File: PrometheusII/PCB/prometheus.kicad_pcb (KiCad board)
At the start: 4 copper layers, 223.5 x 222.3 mm, 240 parts, among them J1 0878311420, J10 Conn_02x02_Odd_Even, J11 Conn_02x02_Odd_Even, J12 Conn_02x08_Odd_Even, J13 Conn_02x08_Odd_Even, J14 Conn_02x08_Odd_Even, J2 Conn_02x08_Odd_Even, J3 Conn_02x02_Odd_Even, J4 Conn_02x02_Odd_Even, J7 Conn_02x08_Odd_Even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

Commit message: Base logic for arc completion works?
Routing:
- net (no net): track 368.4 -> 387.0 mm
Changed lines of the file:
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@@
   (general
     (thickness 1.6)
-    (drawings 239)
-    (tracks 687)
+    (drawings 240)
+    (tracks 689)
     (zones 0)
     (modules 240)
@@
     )
   )
+  (gr_arc (start 99.054 138.009) (end 99.689 136.485) (angle -99.62521694) (layer F.Cu) (width 0.16))
   (gr_circle (center 102.746 98.016) (end 106.646 98.016) (layer B.SilkS) (width 0.16))
   (gr_circle (center 102.746 98.016) (end 106.336 98.016) (layer B.SilkS) (width 0.16))
@@
   (gr_circle (center 106.2735 138.938) (end 107.8435 138.938) (layer B.Cu) (width 0.16))
   (gr_circle (center 106.2735 138.938) (end 107.5235 138.938) (layer B.Cu) (width 0.16))
-  (gr_arc (start 98.9329 138.0998) (end 99.8473 136.6774) (angle 147.2597811) (layer B.Cu) (width 0.16))
+  (gr_arc (start 98.9329 138.0998) (end 99.8473 136.6774) (angle 249.0202197) (layer B.Cu) (width 0.16))
   (gr_arc (start 99.4663 130.8608) (end 100.3807 129.4384) (angle 147.2597811) (layer B.Cu) (width 0.16))
   (gr_arc (start 99.2377 131.2672) (end 99.2377 129.9972) (angle -90) (layer B.Cu) (width 0.16))
@@
   (segment (start 70.198799 115.605993) (end 85.206657 119.741104) (width 0.16) (layer F.Cu) (net 85))
   (segment (start 70.113797 115.914497) (end 85.121655 120.049608) (width 0.16) (layer F.Cu) (net 0))
+  (segment (start 86.750967 139.302139) (end 77.688432 138.62466) (width 0.15) (layer B.Cu) (net 0))
+  (segment (start 86.676185 144.222117) (end 77.255214 143.102682) (width 0.15) (layer B.Cu) (net 0))
   (segment (start 71.108775 101.323762) (end 100.557255 95.046046) (width 0.16) (layer F.Cu) (net 72))
   (segment (start 71.175492 101.636729) (end 100.623973 95.359014) (width 0.16) (layer F.Cu) (net 1))

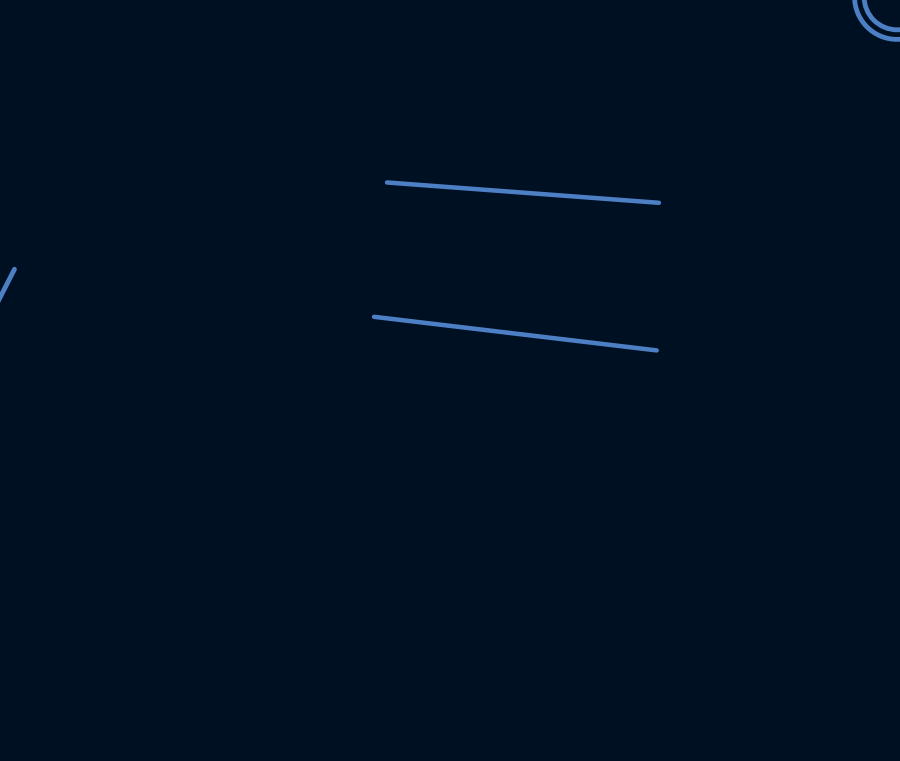
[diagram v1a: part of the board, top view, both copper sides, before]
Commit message: Cleaned up node dialog and added layer select
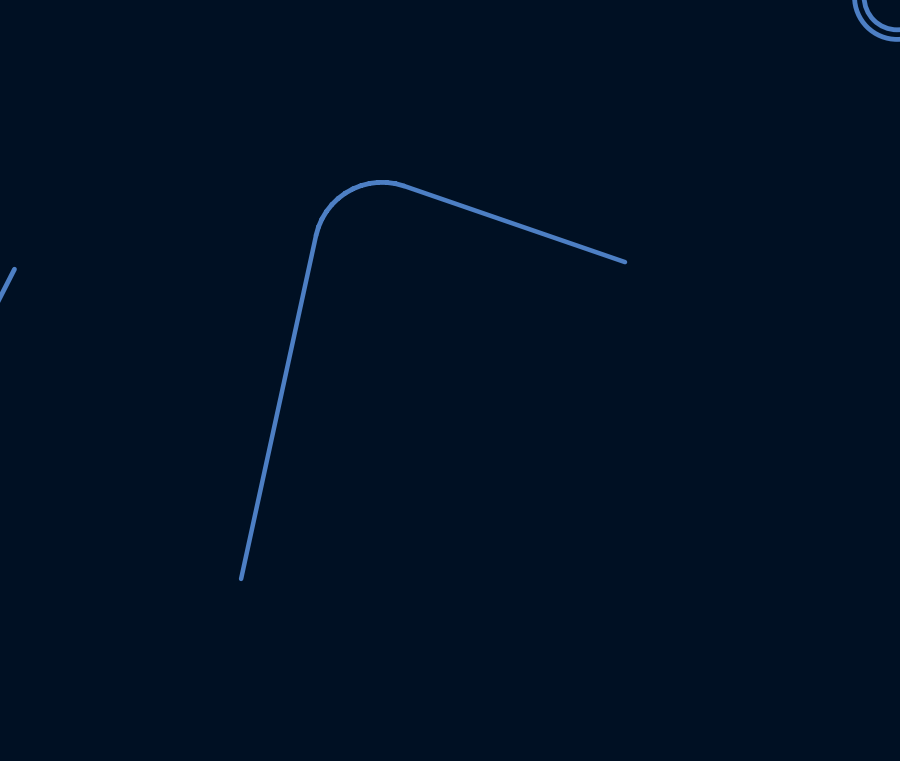
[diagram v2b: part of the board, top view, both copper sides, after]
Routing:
- net +5V: track 41.0 -> 48.8 mm
- net (no net): track 387.0 -> 383.9 mm
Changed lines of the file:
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@@
     (thickness 1.6)
     (drawings 240)
-    (tracks 689)
+    (tracks 702)
     (zones 0)
     (modules 240)
@@
     (35 F.Paste user hide)
     (36 B.SilkS user)
-    (37 F.SilkS user hide)
+    (37 F.SilkS user)
     (38 B.Mask user)
     (39 F.Mask user)
@@
     (44 Edge.Cuts user)
     (45 Margin user)
-    (46 B.CrtYd user)
-    (47 F.CrtYd user)
+    (46 B.CrtYd user hide)
+    (47 F.CrtYd user hide)
     (48 B.Fab user hide)
     (49 F.Fab user hide)
@@
     (solder_mask_min_width 0.25)
     (aux_axis_origin 156.456 180.632)
-    (grid_origin 87.751 140.803)
+    (grid_origin 124.708 144.232)
     (visible_elements 7FFFFFFF)
     (pcbplotparams
@@
   (gr_circle (center 79.7455 125.69) (end 82.4955 125.69) (layer B.SilkS) (width 0.16))
   (gr_circle (center 42.92092 133.598) (end 43.92092 133.598) (layer F.Cu) (width 0.16))
-  (gr_circle (center 86.9187 137.0584) (end 89.1687 137.0584) (layer B.SilkS) (width 0.16))
+  (gr_circle (center 86.354 139.152) (end 88.604 139.152) (layer B.SilkS) (width 0.16))
   (gr_circle (center 86.4107 146.4564) (end 88.6607 146.4564) (layer B.SilkS) (width 0.16))
   (gr_circle (center 77.5207 140.8684) (end 79.7707 140.8684) (layer B.SilkS) (width 0.16))
@@
   (segment (start 70.198799 115.605993) (end 85.206657 119.741104) (width 0.16) (layer F.Cu) (net 85))
   (segment (start 70.113797 115.914497) (end 85.121655 120.049608) (width 0.16) (layer F.Cu) (net 0))
-  (segment (start 86.750967 139.302139) (end 77.688432 138.62466) (width 0.15) (layer B.Cu) (net 0))
-  (segment (start 86.676185 144.222117) (end 77.255214 143.102682) (width 0.15) (layer B.Cu) (net 0))
+  (segment (start 85.621124 141.279297) (end 78.253575 138.741102) (width 0.15) (layer B.Cu) (net 7))
+  (segment (start 72.823349 151.839474) (end 75.322443 140.38864) (width 0.15) (layer B.Cu) (net 0))
+  (segment (start 78.253574 138.741102) (end 77.972011 138.664127) (width 0.16) (layer B.Cu) (net 0))
+  (segment (start 77.972011 138.664127) (end 77.682851 138.62425) (width 0.16) (layer B.Cu) (net 0))
+  (segment (start 77.682851 138.62425) (end 77.390963 138.622143) (width 0.16) (layer B.Cu) (net 0))
+  (segment (start 77.390963 138.622143) (end 77.101258 138.657841) (width 0.16) (layer B.Cu) (net 0))
+  (segment (start 77.101258 138.657841) (end 76.818612 138.730743) (width 0.16) (layer B.Cu) (net 0))
+  (segment (start 76.818612 138.730743) (end 76.547783 138.839623) (width 0.16) (layer B.Cu) (net 0))
+  (segment (start 76.547783 138.839623) (end 76.293328 138.982648) (width 0.16) (layer B.Cu) (net 0))
+  (segment (start 76.293328 138.982648) (end 76.05953 139.15741) (width 0.16) (layer B.Cu) (net 0))
+  (segment (start 76.05953 139.15741) (end 75.850324 139.360969) (width 0.16) (layer B.Cu) (net 0))
+  (segment (start 75.850324 139.360969) (end 75.669231 139.589898) (width 0.16) (layer B.Cu) (net 0))
+  (segment (start 75.669231 139.589898) (end 75.519299 139.840345) (width 0.16) (layer B.Cu) (net 0))
+  (segment (start 75.519299 139.840345) (end 75.403051 140.108094) (width 0.16) (layer B.Cu) (net 0))
+  (segment (start 75.403051 140.108094) (end 75.322443 140.38864) (width 0.16) (layer B.Cu) (net 0))
   (segment (start 71.108775 101.323762) (end 100.557255 95.046046) (width 0.16) (layer F.Cu) (net 72))
   (segment (start 71.175492 101.636729) (end 100.623973 95.359014) (width 0.16) (layer F.Cu) (net 1))

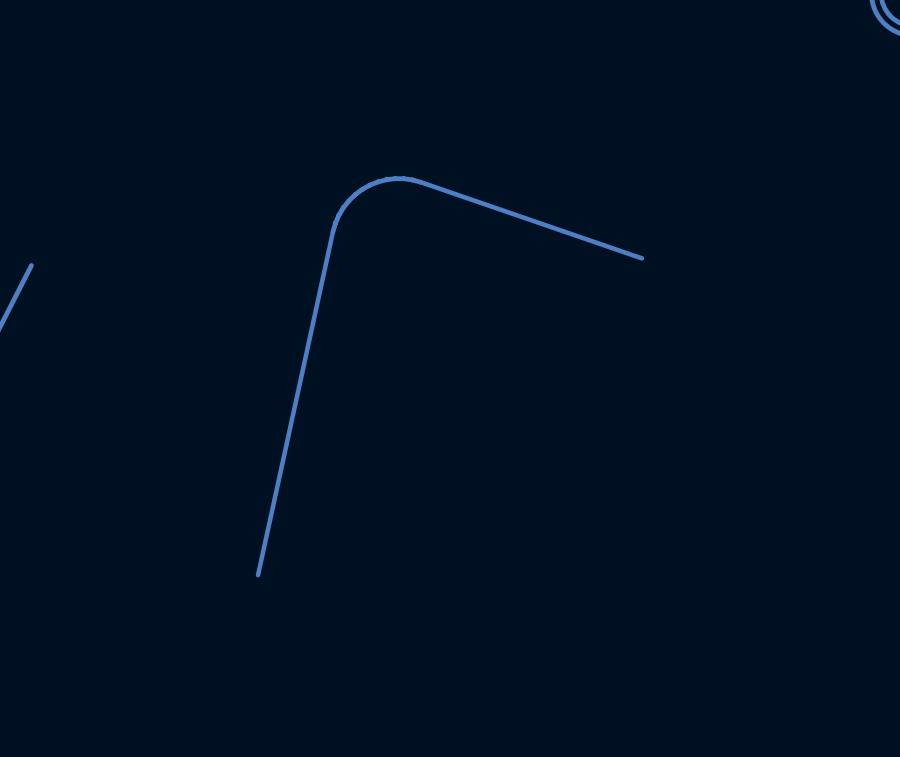
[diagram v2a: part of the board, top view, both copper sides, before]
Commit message: Refactor bus tangent finding to allow for including layers
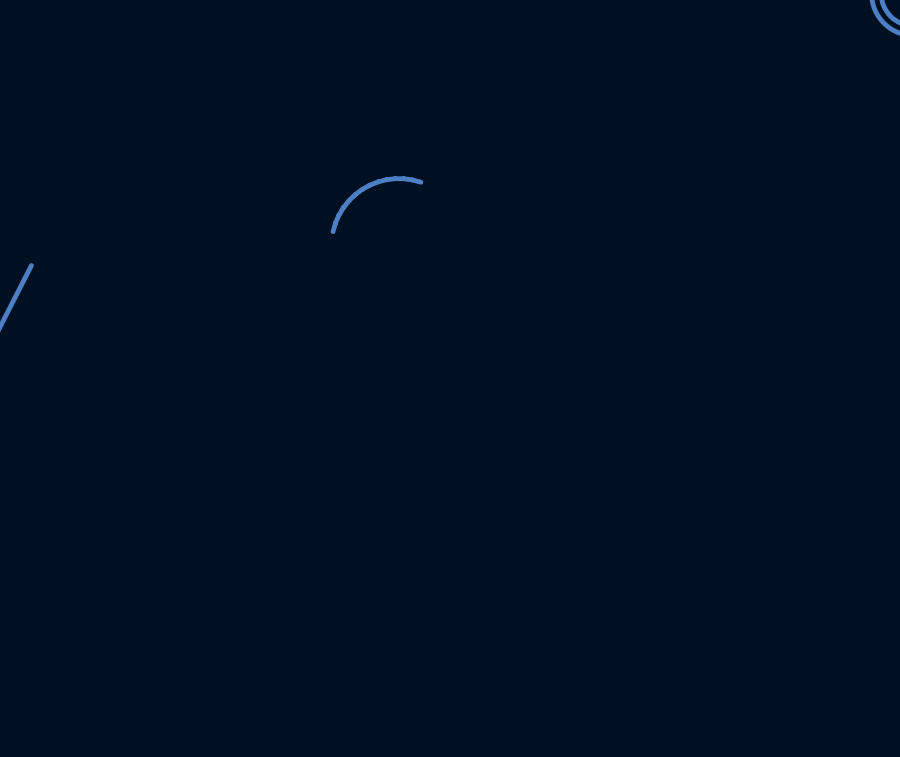
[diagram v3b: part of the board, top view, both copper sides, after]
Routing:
- net (no net): track 383.9 -> 372.2 mm
- net +5V: track 48.8 -> 41.0 mm
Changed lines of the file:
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@@
   (general
     (thickness 1.6)
-    (drawings 240)
-    (tracks 702)
+    (drawings 245)
+    (tracks 700)
     (zones 0)
     (modules 240)
@@
     (solder_mask_min_width 0.25)
     (aux_axis_origin 156.456 180.632)
-    (grid_origin 124.708 144.232)
+    (grid_origin 72.892 145.883)
     (visible_elements 7FFFFFFF)
     (pcbplotparams
@@
     )
   )
+  (gr_circle (center 89.5857 140.2334) (end 92.1557 140.2334) (layer B.SilkS) (width 0.16))
+  (gr_circle (center 89.5857 140.2334) (end 91.8357 140.2334) (layer B.SilkS) (width 0.16))
+  (gr_circle (center 79.8067 149.6314) (end 82.6967 149.6314) (layer B.SilkS) (width 0.16))
+  (gr_circle (center 79.8067 149.6314) (end 82.3767 149.6314) (layer B.SilkS) (width 0.16))
+  (gr_circle (center 79.8067 149.6314) (end 82.0567 149.6314) (layer B.SilkS) (width 0.16))
+  (gr_circle (center 88.8237 148.8694) (end 91.7137 148.8694) (layer B.SilkS) (width 0.16))
+  (gr_circle (center 88.8237 148.8694) (end 91.3937 148.8694) (layer B.SilkS) (width 0.16))
+  (gr_circle (center 88.8237 148.8694) (end 91.0737 148.8694) (layer B.SilkS) (width 0.16))
   (gr_arc (start 99.054 138.009) (end 99.689 136.485) (angle -99.62521694) (layer F.Cu) (width 0.16))
   (gr_circle (center 102.746 98.016) (end 106.646 98.016) (layer B.SilkS) (width 0.16))
@@
   (gr_circle (center 79.7455 125.69) (end 82.4955 125.69) (layer B.SilkS) (width 0.16))
   (gr_circle (center 42.92092 133.598) (end 43.92092 133.598) (layer F.Cu) (width 0.16))
-  (gr_circle (center 86.354 139.152) (end 88.604 139.152) (layer B.SilkS) (width 0.16))
-  (gr_circle (center 86.4107 146.4564) (end 88.6607 146.4564) (layer B.SilkS) (width 0.16))
   (gr_circle (center 77.5207 140.8684) (end 79.7707 140.8684) (layer B.SilkS) (width 0.16))
   (gr_circle (center 77.5207 140.8684) (end 80.0907 140.8684) (layer B.SilkS) (width 0.16))
@@
   (gr_circle (center 58.9787 159.1564) (end 61.5487 159.1564) (layer B.SilkS) (width 0.16))
   (gr_circle (center 58.9787 159.1564) (end 61.8687 159.1564) (layer B.SilkS) (width 0.16))
-  (gr_circle (center 76.5555 152.654) (end 80.3755 152.654) (layer B.SilkS) (width 0.16))
   (gr_circle (center 58.4707 148.4884) (end 61.3607 148.4884) (layer B.SilkS) (width 0.16))
   (gr_circle (center 58.4707 148.4884) (end 61.0407 148.4884) (layer B.SilkS) (width 0.16))
@@
   (segment (start 70.198799 115.605993) (end 85.206657 119.741104) (width 0.16) (layer F.Cu) (net 85))
   (segment (start 70.113797 115.914497) (end 85.121655 120.049608) (width 0.16) (layer F.Cu) (net 0))
-  (segment (start 85.621124 141.279297) (end 78.253575 138.741102) (width 0.15) (layer B.Cu) (net 7))
-  (segment (start 72.823349 151.839474) (end 75.322443 140.38864) (width 0.15) (layer B.Cu) (net 0))
   (segment (start 78.253574 138.741102) (end 77.972011 138.664127) (width 0.16) (layer B.Cu) (net 0))
   (segment (start 77.972011 138.664127) (end 77.682851 138.62425) (width 0.16) (layer B.Cu) (net 0))

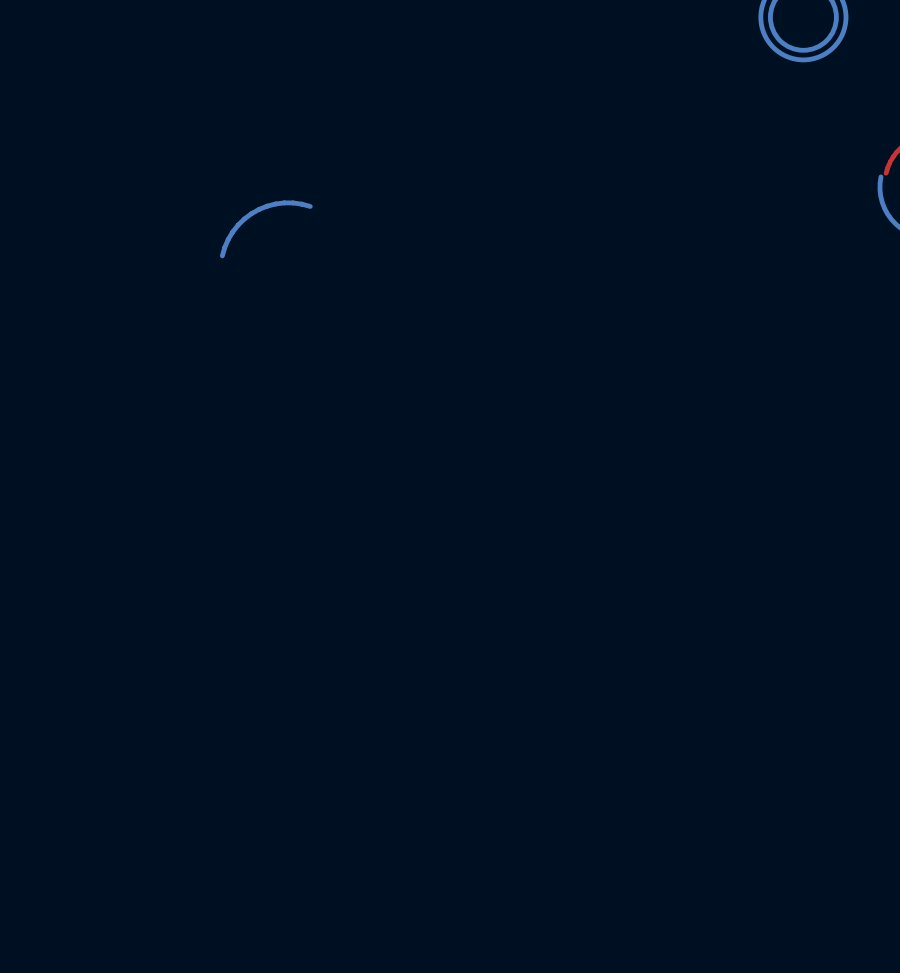
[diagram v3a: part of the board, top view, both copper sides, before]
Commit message: Implemented automatic side selection for circle to circle tangent routing based on bus layer
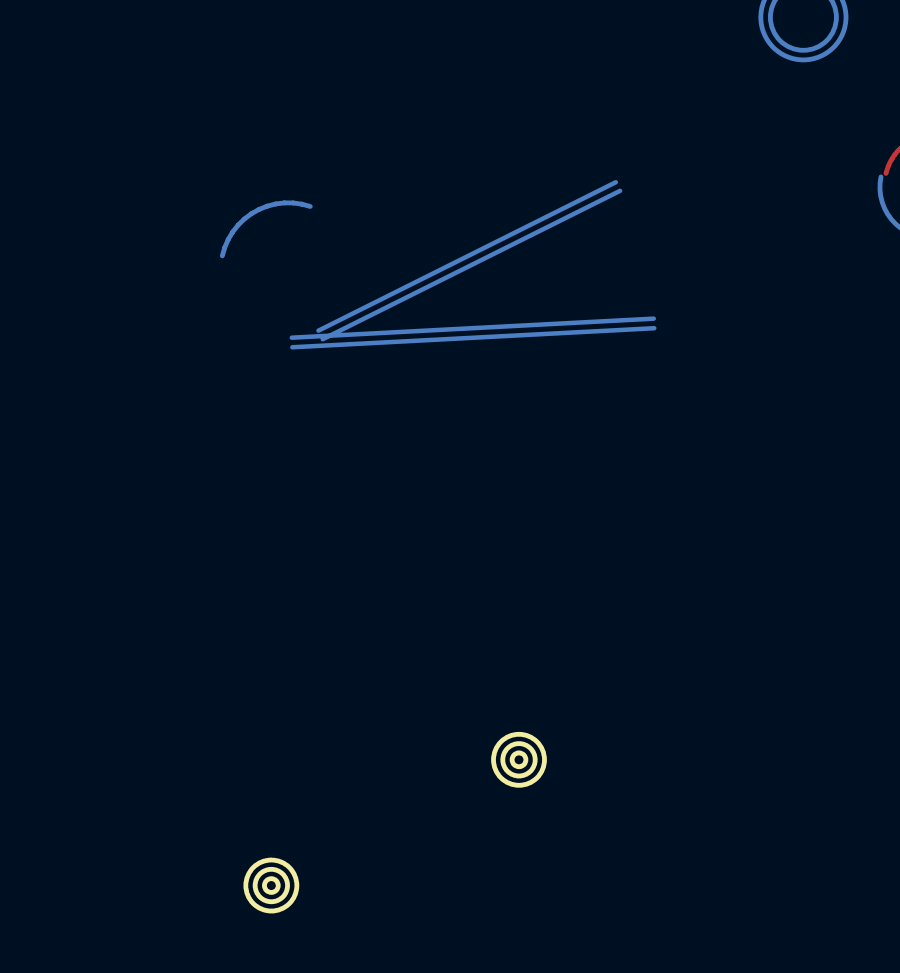
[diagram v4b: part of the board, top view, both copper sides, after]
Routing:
- net (no net): track 372.2 -> 418.6 mm
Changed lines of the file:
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@@
   (general
     (thickness 1.6)
-    (drawings 245)
-    (tracks 700)
+    (drawings 251)
+    (tracks 704)
     (zones 0)
     (modules 240)
@@
     (solder_mask_min_width 0.25)
     (aux_axis_origin 156.456 180.632)
-    (grid_origin 72.892 145.883)
+    (grid_origin 85.084 162.647)
     (visible_elements 7FFFFFFF)
     (pcbplotparams
@@
     )
   )
+  (gr_circle (center 76.956 161.377) (end 77.496 161.377) (layer F.SilkS) (width 0.16))
+  (gr_circle (center 76.956 161.377) (end 77.806 161.377) (layer F.SilkS) (width 0.16))
+  (gr_circle (center 76.956 161.377) (end 77.186 161.377) (layer F.SilkS) (width 0.16))
+  (gr_circle (center 85.211 157.186) (end 86.061 157.186) (layer F.SilkS) (width 0.16))
+  (gr_circle (center 85.211 157.186) (end 85.751 157.186) (layer F.SilkS) (width 0.16))
+  (gr_circle (center 85.211 157.186) (end 85.441 157.186) (layer F.SilkS) (width 0.16))
   (gr_circle (center 89.5857 140.2334) (end 92.1557 140.2334) (layer B.SilkS) (width 0.16))
   (gr_circle (center 89.5857 140.2334) (end 91.8357 140.2334) (layer B.SilkS) (width 0.16))
@@
   (segment (start 75.519299 139.840345) (end 75.403051 140.108094) (width 0.16) (layer B.Cu) (net 0))
   (segment (start 75.403051 140.108094) (end 75.322443 140.38864) (width 0.16) (layer B.Cu) (net 0))
+  (segment (start 78.668446 143.167873) (end 88.580863 138.220242) (width 0.15) (layer B.Cu) (net 0))
+  (segment (start 88.437953 137.933926) (end 78.525536 142.881557) (width 0.15) (layer B.Cu) (net 0))
+  (segment (start 89.703957 142.48029) (end 77.638957 143.11529) (width 0.15) (layer B.Cu) (net 0))
+  (segment (start 89.720776 142.799847) (end 77.655776 143.434847) (width 0.15) (layer B.Cu) (net 0))
   (segment (start 71.108775 101.323762) (end 100.557255 95.046046) (width 0.16) (layer F.Cu) (net 72))
   (segment (start 71.175492 101.636729) (end 100.623973 95.359014) (width 0.16) (layer F.Cu) (net 1))
